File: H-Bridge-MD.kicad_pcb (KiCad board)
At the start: 2 copper layers, 85 x 50 mm, 69 parts, among them IC1 SI8650AB-B-IS1, IC2 A3921KLPTR-T, IC3 SI8650AB-B-IS1, IC4 A3921KLPTR-T, J1 Conn_01x02, J2 Conn_01x03, J3 Conn_01x05, J4 Conn_01x02, J5 Bus_mechaken_PCIexpress_x16_1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, Q1 NVMFD5C650NLWFT1G, Q2 NVMFD5C650NLWFT1G, Q3 NVMFD5C650NLWFT1G, Q4 NVMFD5C650NLWFT1G, SW1 SW_Push, U1 LDL1117S33TR_SOT223-4, U2 STM32F042K6Tx, U3 MCP2562-E-SN

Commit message: remove RESET_SW
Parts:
- removed C3: 0.1uF, Capacitor_SMD:C_0805_2012Metric
- removed D5: LED, LED_SMD:LED_0603_1608Metric
- removed R11, R9: 10K, Resistor_SMD:R_0603_1608Metric
- removed SW1: SW_Push, SamacSys_Parts:PTS647SM38SMTR2LFS
- J2: footprint Connector_JST:JST_XH_B3B-XH-A_1x03_P2.50mm_Vertical -> Connector_PinHeader_2.54mm:PinHeader_1x03_P2.54mm_Vertical; moved to F.Cu
- J3: footprint Connector_JST:JST_XH_B5B-XH-A_1x05_P2.50mm_Vertical -> Connector_PinHeader_2.54mm:PinHeader_1x05_P2.54mm_Vertical; moved to B.Cu
- Q1, Q2, Q3, Q4: value NVMFD5C650NLWFT1G -> NVMFD5C446NT1G
- moved J3 2.44 mm to (86.4, 47.3), turned to 90 degrees
- moved J2 1.27 mm to (72.7, 47.3), turned to 270 degrees
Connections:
- Q2 pad 6: SB_1 -> SA_1
- Q3 pad 6: SB_0 -> SA_0
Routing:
- net SB_0: track 35.8 -> 54.9 mm, vias 121 -> 109
- net SB_1: track 33.7 -> 51.0 mm, vias 118 -> 103
- net NRST: track 58.2 -> 47.3 mm, vias 3 -> 2
- net +3V3: track 117.7 -> 107.5 mm, vias 4 -> 2
- net SA_1: track 29.4 -> 38.1 mm, vias 128 -> 116
- net SA_0: track 27.8 -> 34.6 mm, vias 125 -> 105
- net VCC: track 18.2 -> 24.0 mm, vias 409 -> 414
- net GNDPWR: track 110.9 -> 115.8 mm, vias 240 -> 254
- net GLB_0: track 52.2 -> 56.8 mm
- net GHB_0: track 30.9 -> 35.5 mm
- net GLA_0: track 51.9 -> 55.6 mm
- net Net-(D5-Pad2): track 2.67 -> 0.00 mm
- net VCP_RX: track 20.0 -> 17.6 mm, vias 3 -> 2
- net GND: track 4.78 -> 2.83 mm, vias 31 -> 30
- net VREG_0: track 8.55 -> 6.69 mm
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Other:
- board text removed: "RESET"

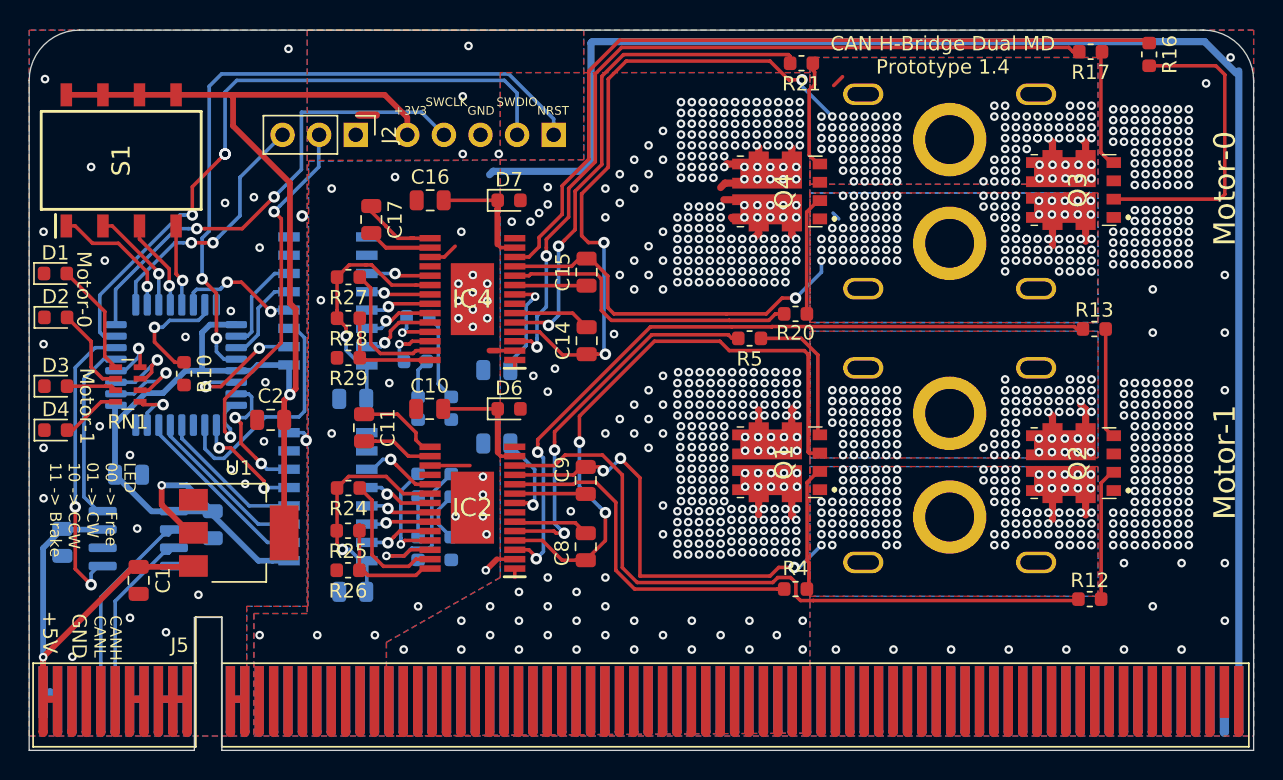
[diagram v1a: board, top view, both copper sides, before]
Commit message: Fix FET via
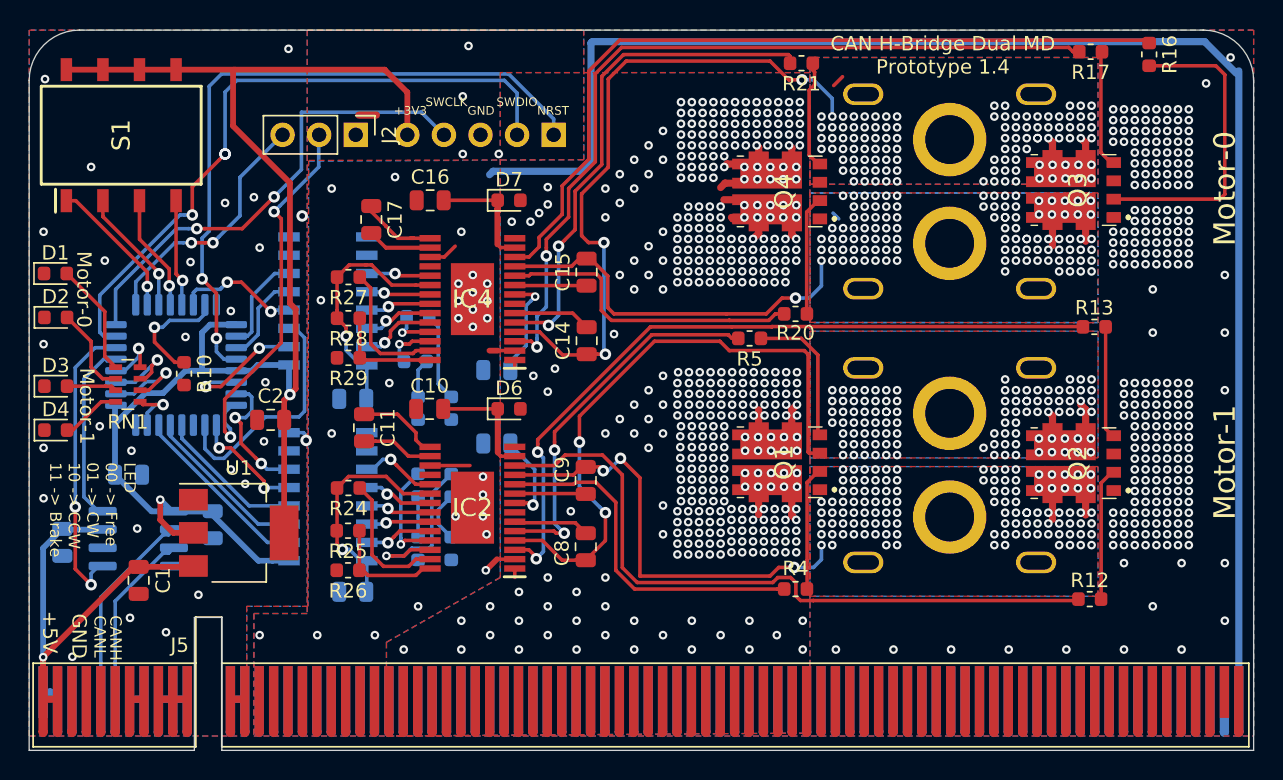
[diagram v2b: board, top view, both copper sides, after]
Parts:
- moved S1 1.75 mm to (56.4, 47.3)
- moved R13 0.15 mm to (123.9, 60.6)
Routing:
- net +3V3: track 107.5 -> 110.4 mm
- net DIP_SW_4: track 5.69 -> 7.44 mm
- net DIP_SW_3: track 6.53 -> 8.28 mm
- net DIP_SW_2: track 7.46 -> 8.83 mm
- net DIP_SW_1: track 9.22 -> 9.95 mm
- net SA_1: track 38.1 -> 38.7 mm
- net SA_0: track 34.6 -> 35.1 mm
- net GND: vias 30 -> 31

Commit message: add 3V3LDO & pad
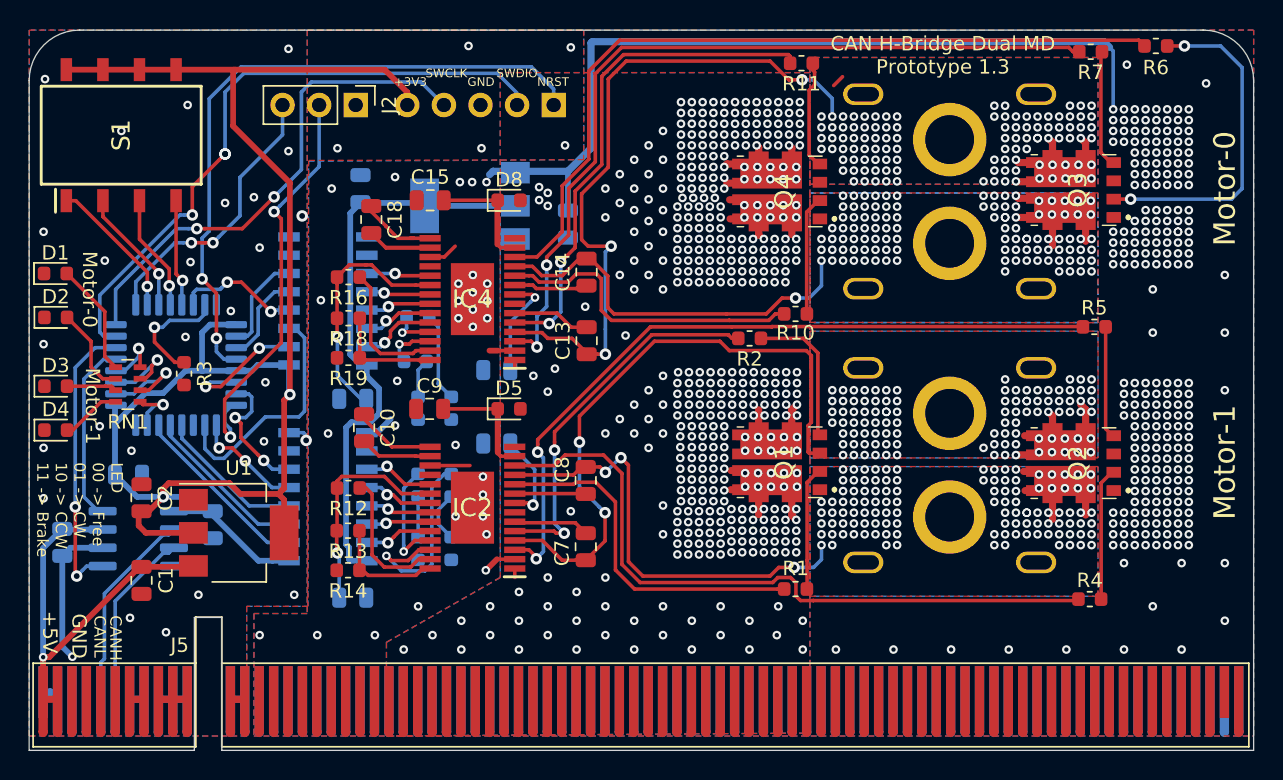
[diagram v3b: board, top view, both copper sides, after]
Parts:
- added C16: 1uF, Capacitor_SMD:C_0805_2012Metric, B.Cu at (87.4, 53.5)
- added C17: 4.7uF, Capacitor_SMD:C_0805_2012Metric, B.Cu at (73.0, 51.0)
- added U4: LDL1117S33TR_SOT223-4, Package_TO_SOT_SMD:SOT-223-3_TabPin2, B.Cu at (80.6, 52.2)
- moved C2 10.5 mm to (57.8, 72.5), turned to 270 degrees
- moved J2 2.07 mm to (72.7, 45.2)
- moved J3 2.07 mm to (86.4, 45.2)
- moved R6 0.75 mm to (128.2, 41.1), turned to 0 degrees
- moved C11 0.41 mm to (72.5, 79.4), turned to 0 degrees
- moved C1 0.20 mm to (57.8, 78.2)
- renumbered C11 to C10, C12 to C11, C13 to C12, C14 to C13, C15 to C14, C16 to C15, C17 to C18, C18 to C19, C4 to C3, C5 to C4, C6 to C5, C7 to C6, C8 to C7, C9 to C8, C10 to C9, D11 to D10, D6 to D5, D8 to D6, D9 to D7, D7 to D8, D10 to D9, R4 to R1, R20 to R10, R21 to R11, R24 to R12, R25 to R13, R26 to R14, R32 to R15, R27 to R16, R33 to R17, R28 to R18, R29 to R19, R5 to R2, R10 to R3, R12 to R4, R13 to R5, R16 to R6, R17 to R7, R30 to R8, R31 to R9
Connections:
- C11 pad 1: MD_V5_1 -> Net-(C11-Pad1)
- C19 pad 1: MD_V5_0 -> Net-(C19-Pad1)
- IC1 pad 16: MD_V5_1 -> MD_3V3
- IC2 pad 20: MD_V5_1 -> Net-(C11-Pad1)
- IC3 pad 16: MD_V5_0 -> MD_3V3
- IC4 pad 20: MD_V5_0 -> Net-(C19-Pad1)
- R12 pad 2: MD_V5_1 -> Net-(C11-Pad1)
- R13 pad 2: MD_V5_1 -> Net-(C11-Pad1)
- R16 pad 2: MD_V5_0 -> Net-(C19-Pad1)
- R18 pad 2: MD_V5_0 -> Net-(C19-Pad1)
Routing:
- net GNDPWR: track 115.8 -> 69.4 mm, vias 254 -> 257
- net MD_3V3: track 0.00 -> 40.1 mm
- net MD_V5_0: track 17.0 -> 0.00 mm, vias 1 -> 0
- net Net-(C19-Pad1): track 0.00 -> 16.9 mm, vias 0 -> 1
- net MD_V5_1: track 15.9 -> 0.00 mm, vias 1 -> 0
- net Net-(C11-Pad1): track 0.00 -> 15.2 mm, vias 0 -> 1
- net GND: track 2.83 -> 11.9 mm, vias 31 -> 32
- net +3V3: track 110.4 -> 119.4 mm
- net SB_0: track 55.4 -> 58.1 mm
- net /SWDIO: track 45.9 -> 43.4 mm
- net MD_FF1_1: track 12.2 -> 14.3 mm
- net VCP_TX: track 27.2 -> 29.2 mm
- net VCP_RX: track 17.6 -> 19.6 mm
- net VCC: track 24.0 -> 26.0 mm, vias 414 -> 435
- net SA_0: track 35.1 -> 37.1 mm, vias 105 -> 107
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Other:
- board text added: "CAN H-Bridge Dual MD Prototype 1.3"
- board text removed: "CAN H-Bridge Dual MD Prototype 1.4"

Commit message: Prototype 1.3
FusionPCB(12/12)
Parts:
- renumbered D8 to D10, D9 to D6, D10 to D7, D6 to D8, D7 to D9, R8 to R10, R9 to R11, R10 to R12, R11 to R13, R12 to R14, R13 to R15, R14 to R16, R16 to R17, R15 to R8, R17 to R9
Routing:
- net MD_FF1_1: track 14.3 -> 12.5 mm
- net Net-(C11-Pad1): track 15.2 -> 16.4 mm
- net MD_FF2_1: track 7.90 -> 6.74 mm
- net Net-(C19-Pad1): track 16.9 -> 18.0 mm
- net GLB_0: track 56.8 -> 57.5 mm
- net MD_RESET_1: track 4.74 -> 5.25 mm
- net GNDPWR: vias 257 -> 259
- net GND: vias 32 -> 34
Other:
- board text added: "CAN H-Bridge Dual MD Prototype 1.2"
- board text removed: "CAN H-Bridge Dual MD Prototype 1.3"

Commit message: fix bootstrap capacitor
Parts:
- C13, C14, C7, C8: value 0.1uF -> 4.7uF
- U1: value LDL1117S33TR_SOT223-4 -> LDL1117S33R_SOT223-4
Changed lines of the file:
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@@
     (add_net "Net-(D8-Pad2)")
     (add_net "Net-(D9-Pad2)")
+    (add_net "Net-(IC1-Pad10)")
+    (add_net "Net-(IC1-Pad7)")
+    (add_net "Net-(IC2-Pad14)")
+    (add_net "Net-(IC2-Pad18)")
     (add_net "Net-(IC2-Pad27)")
     (add_net "Net-(IC2-Pad28)")
+    (add_net "Net-(IC2-Pad7)")
+    (add_net "Net-(IC3-Pad10)")
+    (add_net "Net-(IC3-Pad7)")
+    (add_net "Net-(IC4-Pad14)")
+    (add_net "Net-(IC4-Pad18)")
     (add_net "Net-(IC4-Pad27)")
     (add_net "Net-(IC4-Pad28)")
+    (add_net "Net-(IC4-Pad7)")
     (add_net "Net-(J5-PadA5)")
     (add_net "Net-(J5-PadA6)")
@@
     (add_net "Net-(Q4-Pad2)")
     (add_net "Net-(Q4-Pad4)")
+    (add_net "Net-(U2-Pad11)")
     (add_net SA_0)
     (add_net SA_1)
@@
       (effects (font (size 1 1) (thickness 0.15)))
     )
-    (fp_text value LDL1117S33TR_SOT223-4 (at 0 4.5) (layer F.Fab)
+    (fp_text value LDL1117S33R_SOT223-4 (at 0 4.5) (layer F.Fab)
       (effects (font (size 1 1) (thickness 0.15)))
     )
@@
       (effects (font (size 1 1) (thickness 0.15)))
     )
-    (fp_text value 0.1uF (at 0 1.65 90) (layer F.Fab)
+    (fp_text value 4.7uF (at 0 1.65 90) (layer F.Fab)
       (effects (font (size 1 1) (thickness 0.15)))
     )
@@
       (effects (font (size 1 1) (thickness 0.15)))
     )
-    (fp_text value 0.1uF (at 0 1.65 90) (layer F.Fab)
+    (fp_text value 4.7uF (at 0 1.65 90) (layer F.Fab)
       (effects (font (size 1 1) (thickness 0.15)))
     )
@@
       (effects (font (size 1 1) (thickness 0.15)))
     )
-    (fp_text value 0.1uF (at 0 1.65 270) (layer F.Fab)
+    (fp_text value 4.7uF (at 0 1.65 270) (layer F.Fab)
       (effects (font (size 1 1) (thickness 0.15)))
     )
@@
       (effects (font (size 1 1) (thickness 0.15)))
     )
-    (fp_text value 0.1uF (at 0 1.65 90) (layer F.Fab)
+    (fp_text value 4.7uF (at 0 1.65 90) (layer F.Fab)
       (effects (font (size 1 1) (thickness 0.15)))
     )

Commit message: update
change MD name
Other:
- board text added: "CAN Dual H-Bridge MDU Prototype 1.3"
- board text removed: "CAN H-Bridge Dual MD Prototype 1.2"
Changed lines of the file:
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@@
     (add_net "Net-(D8-Pad2)")
     (add_net "Net-(D9-Pad2)")
-    (add_net "Net-(IC1-Pad10)")
-    (add_net "Net-(IC1-Pad7)")
-    (add_net "Net-(IC2-Pad14)")
-    (add_net "Net-(IC2-Pad18)")
     (add_net "Net-(IC2-Pad27)")
     (add_net "Net-(IC2-Pad28)")
-    (add_net "Net-(IC2-Pad7)")
-    (add_net "Net-(IC3-Pad10)")
-    (add_net "Net-(IC3-Pad7)")
-    (add_net "Net-(IC4-Pad14)")
-    (add_net "Net-(IC4-Pad18)")
     (add_net "Net-(IC4-Pad27)")
     (add_net "Net-(IC4-Pad28)")
-    (add_net "Net-(IC4-Pad7)")
     (add_net "Net-(J5-PadA5)")
     (add_net "Net-(J5-PadA6)")
@@
     (add_net "Net-(Q4-Pad2)")
     (add_net "Net-(Q4-Pad4)")
-    (add_net "Net-(U2-Pad11)")
     (add_net SA_0)
     (add_net SA_1)
@@
   (gr_line (start 63.373 80.772) (end 63.373 90) (layer Edge.Cuts) (width 0.05))
   (gr_line (start 61.468 90) (end 61.468 80.772) (layer Edge.Cuts) (width 0.05))
-  (gr_text "CAN H-Bridge Dual MD\nPrototype 1.2" (at 113.43 41.75) (layer F.SilkS)
+  (gr_text "CAN Dual H-Bridge MDU\nPrototype 1.3" (at 113.43 41.75) (layer F.SilkS)
     (effects (font (size 1 1) (thickness 0.15)))
   )
